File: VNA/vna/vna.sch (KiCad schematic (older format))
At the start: 4 parts, among them J1 USB_B_Micro, J2 Battery Cell Connection, J3 Pt1, J4 Pt2

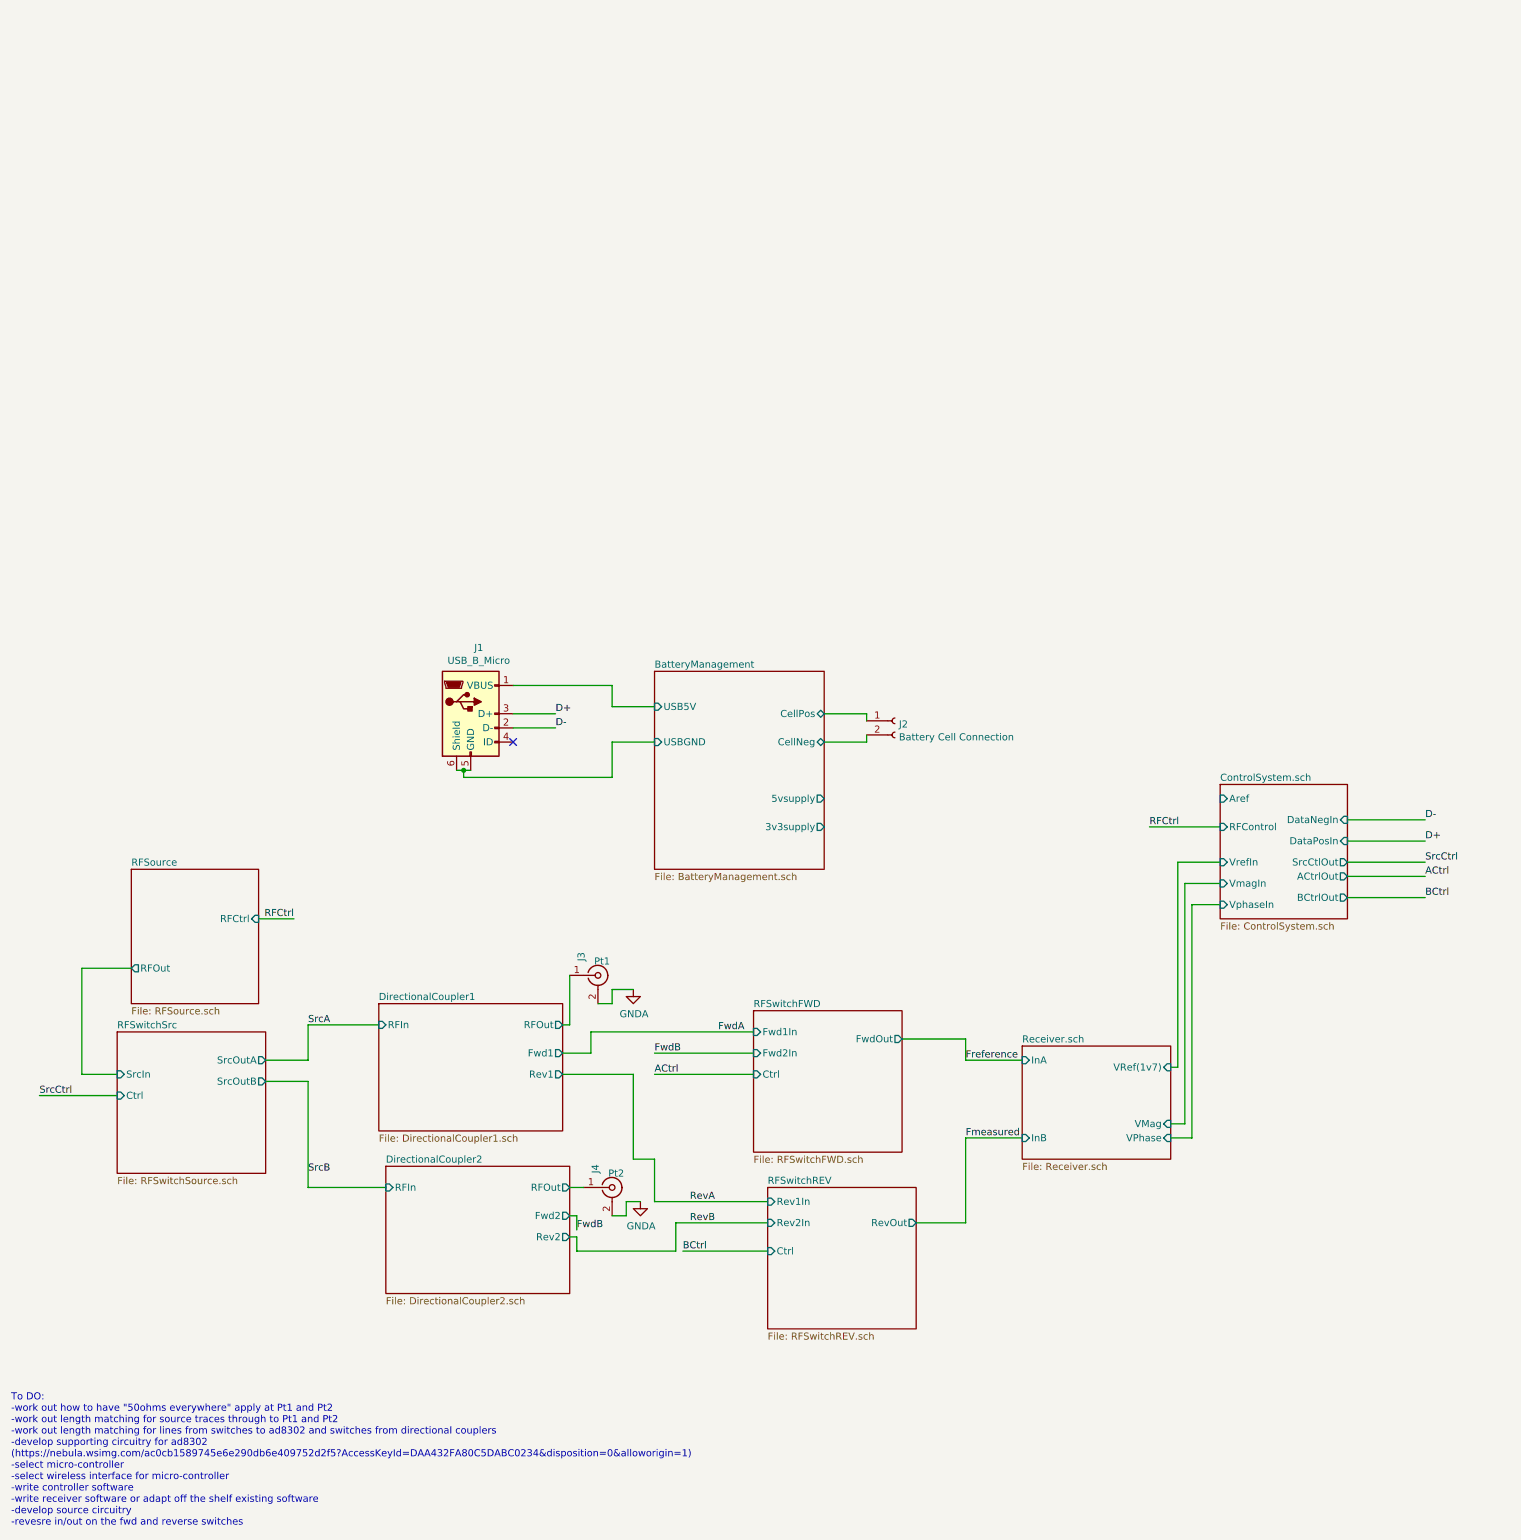
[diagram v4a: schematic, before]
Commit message: finished controller, chose compatible switches
controller and rf switches have been completed.

ToDo: finish filter design for RF Source, add auto gain control
ToDo: finish directional coupler footprints
ToDo: PCB Layout
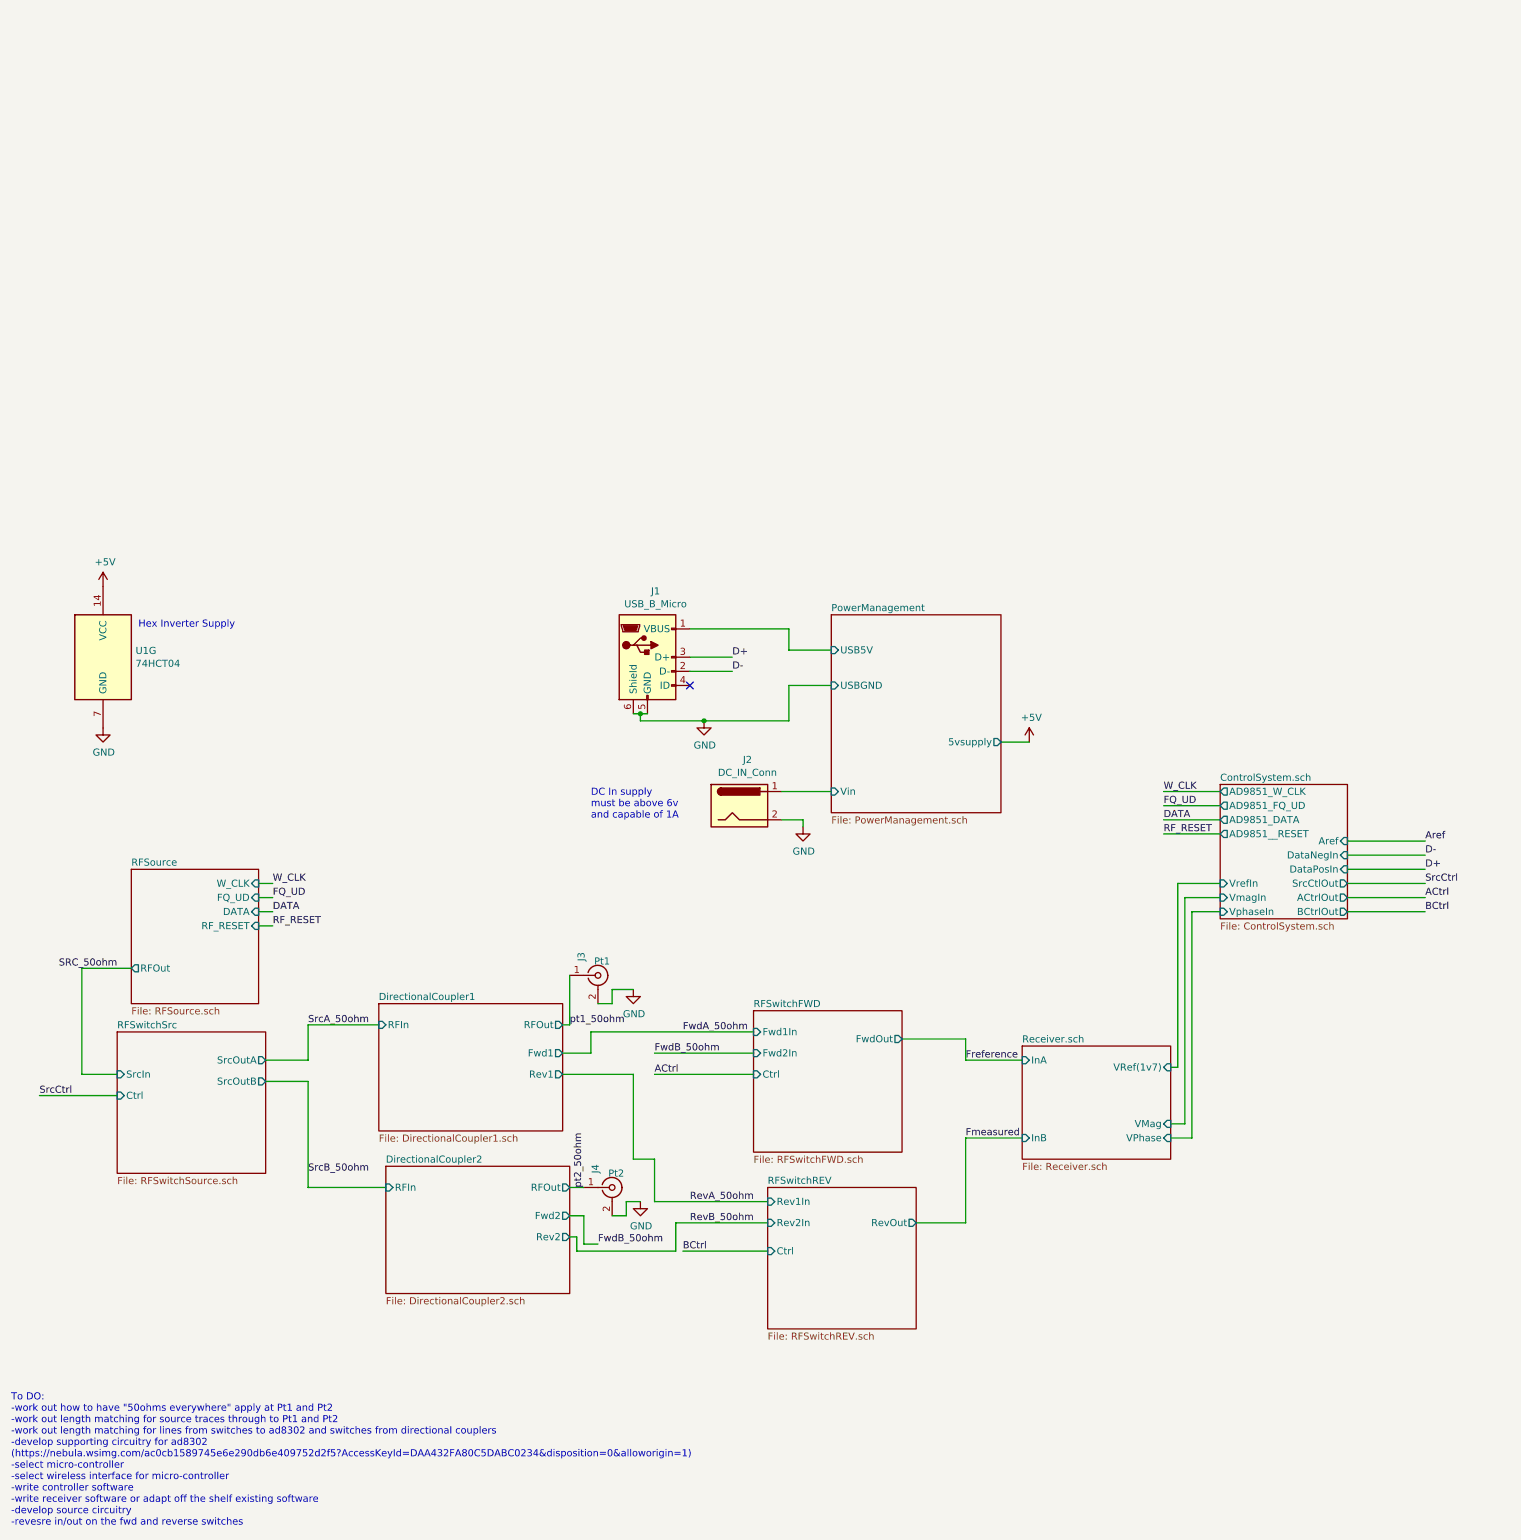
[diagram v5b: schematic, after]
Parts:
- removed J2: Battery Cell Connection, symbol Connector:Conn_01x02_Female
- added J2: DC_IN_Conn, Connector_BarrelJack:BarrelJack_Wuerth_6941xx301002, symbol Connector:Barrel_Jack
- added U1: 74HCT04, Package_SO:SOIC-14_3.9x8.7mm_P1.27mm, symbol 74xx:74HCT04
- J1: footprint (none) -> Connector_USB:USB_Micro-B_Amphenol_10103594-0001LF_Horizontal
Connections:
- net GNDA is gone; now on net GND: J3.2 (Ext), J4.2 (Ext)
- net BatteryManagement/USB5V renamed PowerManagement/USB5V
- net BatteryManagement/USBGND renamed GND
- net GND: now also J2.2, U1.7 (GND)
- net DirectionalCoupler1/RFOut renamed pt1_50ohm
- net DirectionalCoupler2/RFOut renamed pt2_50ohm
- new net +5V: U1.14 (VCC)
- new net PowerManagement/Vin: J2.1
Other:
- note added: "DC In supply \nmust be above 6v\nand capable of 1A"
- note added: "Hex Inverter Supply"
- moved on the sheet: J1

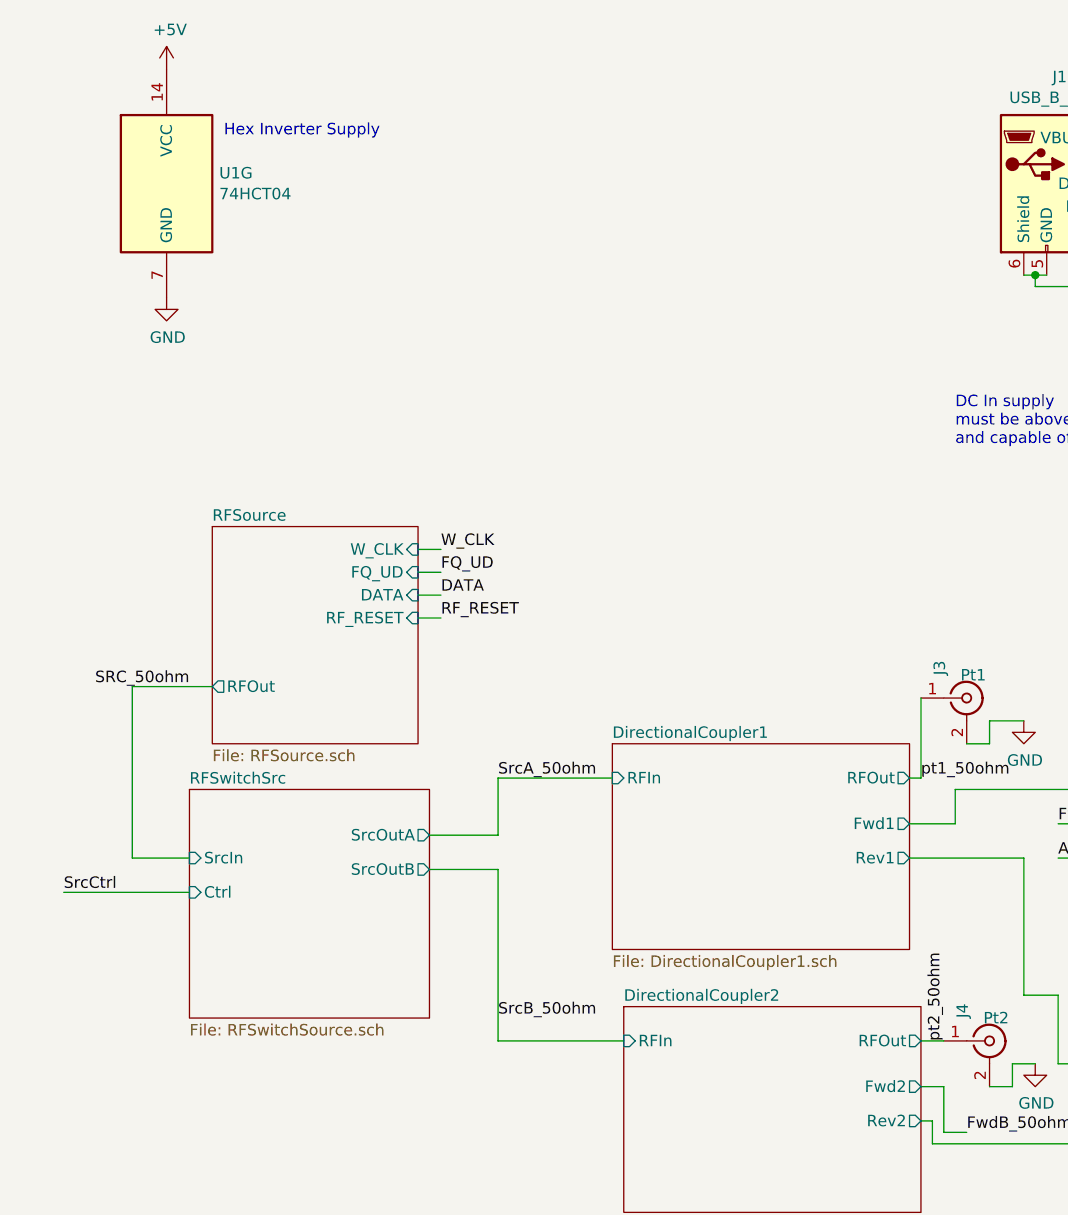
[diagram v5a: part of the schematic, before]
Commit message: custom footprint for couplers, added decoupling caps
added custom footprint for directional couplers - will need to verify it

added decoupling caps to ad9851
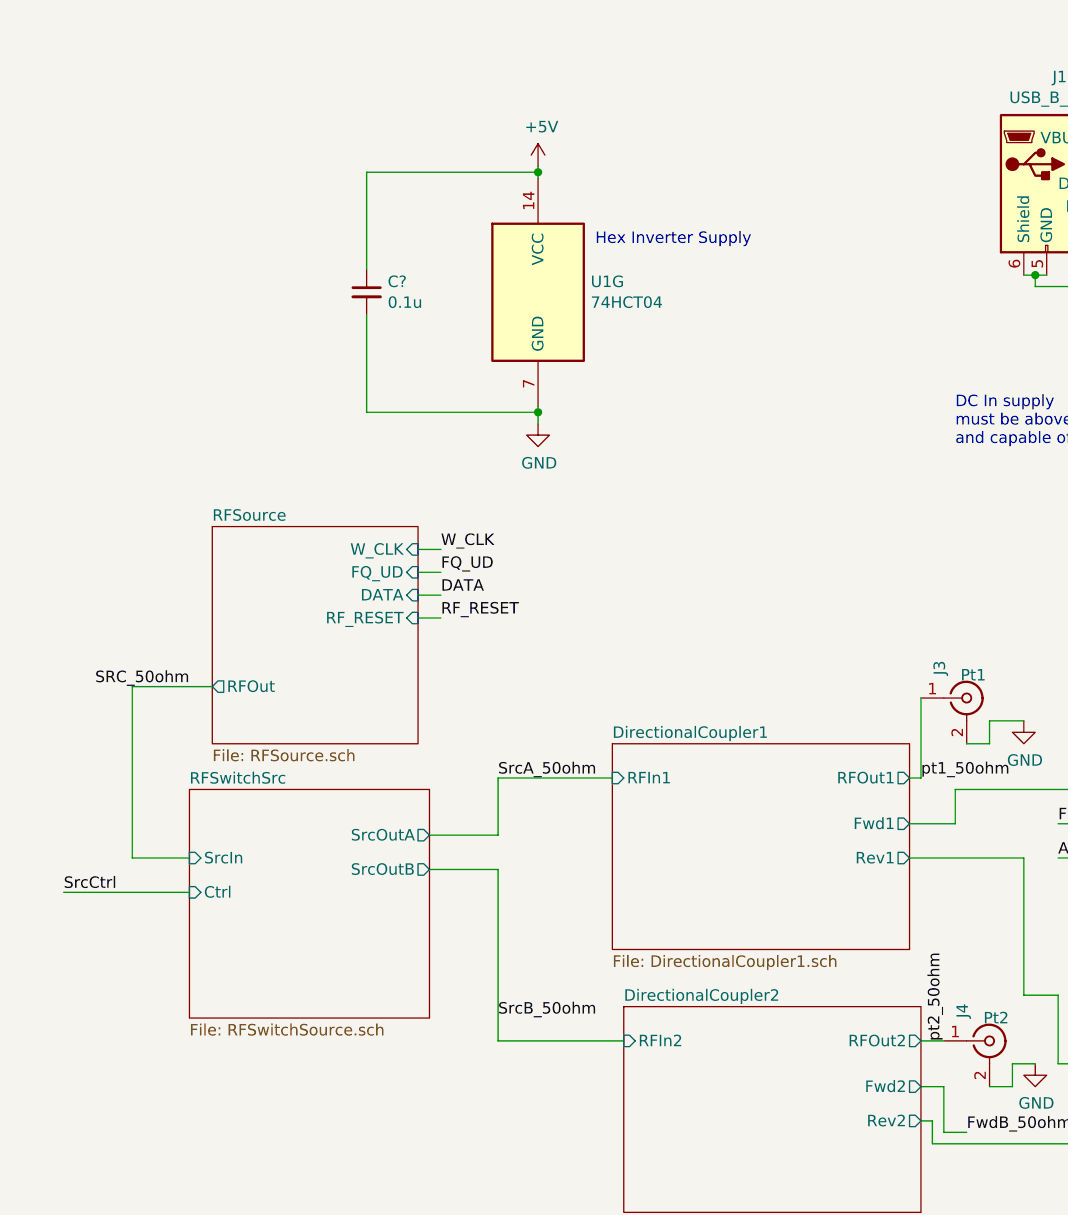
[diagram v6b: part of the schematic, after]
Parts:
- added C?: 0.1u, symbol Device:C_Small
- J3, J4: footprint (none) -> Connector_Coaxial:BNC_Amphenol_B6252HB-NPP3G-50_Horizontal
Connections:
- net +5V: now also C?.1
- net GND: now also C?.2
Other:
- moved on the sheet: U1G
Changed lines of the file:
@@
 F 0 "J3" V 4732 3750 50  0000 L CNN
 F 1 "Pt1" H 4823 3750 50  0000 L CNN
-F 2 "" H 4850 3650 50  0001 C CNN
+F 2 "Connector_Coaxial:BNC_Amphenol_B6252HB-NPP3G-50_Horizontal" H 4850 3650 50  0001 C CNN
 F 3 " ~" H 4850 3650 50  0001 C CNN
 	1    4850 3650
@@
 F0 "DirectionalCoupler1" 50
 F1 "DirectionalCoupler1.sch" 50
-F2 "RFIn" I L 3300 4000 50
-F3 "RFOut" O R 4600 4000 50
+F2 "RFOut1" O R 4600 4000 50
+F3 "RFIn1" I L 3300 4000 50
 F4 "Fwd1" O R 4600 4200 50
 F5 "Rev1" O R 4600 4350 50
-$EndSheet
-$Sheet
-S 3350 5000 1300 900
-U 5CC6A089
-F0 "DirectionalCoupler2" 50
-F1 "DirectionalCoupler2.sch" 50
-F2 "RFIn" I L 3350 5150 50
-F3 "RFOut" O R 4650 5150 50
-F4 "Fwd2" O R 4650 5350 50
-F5 "Rev2" O R 4650 5500 50
 $EndSheet
 $Sheet
@@
 F 0 "J4" V 4832 5250 50  0000 L CNN
 F 1 "Pt2" H 4923 5250 50  0000 L CNN
-F 2 "" H 4950 5150 50  0001 C CNN
+F 2 "Connector_Coaxial:BNC_Amphenol_B6252HB-NPP3G-50_Horizontal" H 4950 5150 50  0001 C CNN
 F 3 " ~" H 4950 5150 50  0001 C CNN
 	1    4950 5150
@@
 L 74xx:74HCT04 U1
 U 7 1 5D8669BB
-P 1350 1400
-F 0 "U1" H 1580 1446 50  0000 L CNN
-F 1 "74HCT04" H 1580 1355 50  0000 L CNN
-F 2 "Package_SO:SOIC-14_3.9x8.7mm_P1.27mm" H 1350 1400 50  0001 C CNN
-F 3 "https://assets.nexperia.com/documents/data-sheet/74HC_HCT04.pdf" H 1350 1400 50  0001 C CNN
-	7    1350 1400
+P 2975 1875
+F 0 "U1" H 3205 1921 50  0000 L CNN
+F 1 "74HCT04" H 3205 1830 50  0000 L CNN
+F 2 "Package_SO:SOIC-14_3.9x8.7mm_P1.27mm" H 2975 1875 50  0001 C CNN
+F 3 "https://assets.nexperia.com/documents/data-sheet/74HC_HCT04.pdf" H 2975 1875 50  0001 C CNN
+	7    2975 1875
 	1    0    0    -1
 $EndComp
@@
 L power:GND #PWR03
 U 1 1 5D86818F
-P 1350 1900
-F 0 "#PWR03" H 1350 1650 50  0001 C CNN
-F 1 "GND" H 1355 1727 50  0000 C CNN
-F 2 "" H 1350 1900 50  0001 C CNN
-F 3 "" H 1350 1900 50  0001 C CNN
-	1    1350 1900
+P 2975 2450
+F 0 "#PWR03" H 2975 2200 50  0001 C CNN
+F 1 "GND" H 2980 2277 50  0000 C CNN
+F 2 "" H 2975 2450 50  0001 C CNN
+F 3 "" H 2975 2450 50  0001 C CNN
+	1    2975 2450
 	1    0    0    -1
 $EndComp
@@
 L power:+5V #PWR?
 U 1 1 5D869326
-P 1350 900
+P 2975 1325
 AR Path="/5CD1CF30/5D869326" Ref="#PWR?"  Part="1"
 AR Path="/5D869326" Ref="#PWR01"  Part="1"
-F 0 "#PWR01" H 1350 750 50  0001 C CNN
-F 1 "+5V" H 1365 1073 50  0000 C CNN
-F 2 "" H 1350 900 50  0001 C CNN
-F 3 "" H 1350 900 50  0001 C CNN
-	1    1350 900
+F 0 "#PWR01" H 2975 1175 50  0001 C CNN
+F 1 "+5V" H 2990 1498 50  0000 C CNN
+F 2 "" H 2975 1325 50  0001 C CNN
+F 3 "" H 2975 1325 50  0001 C CNN
+	1    2975 1325
 	1    0    0    -1
 $EndComp
@@
 Text Notes 4800 2550 0    50   ~ 0
 DC In supply \nmust be above 6v\nand capable of 1A
-Text Notes 1600 1200 0    50   ~ 0
+Text Notes 3225 1675 0    50   ~ 0
 Hex Inverter Supply
 Wire Wire Line
@@
 Wire Wire Line
 	2450 3300 2550 3300
+$Sheet
+S 3350 5000 1300 900
+U 5CC6A089
+F0 "DirectionalCoupler2" 50
+F1 "DirectionalCoupler2.sch" 50
+F2 "Fwd2" O R 4650 5350 50
+F3 "Rev2" O R 4650 5500 50
+F4 "RFOut2" O R 4650 5150 50
+F5 "RFIn2" I L 3350 5150 50
+$EndSheet
+$Comp
+L Device:C_Small C?
+U 1 1 5D96EE93
+P 2225 1875
+F 0 "C?" H 2317 1921 50  0000 L CNN
+F 1 "0.1u" H 2317 1830 50  0000 L CNN
+F 2 "" H 2225 1875 50  0001 C CNN
+F 3 "~" H 2225 1875 50  0001 C CNN
+	1    2225 1875
+	1    0    0    -1
+$EndComp
+Wire Wire Line
+	2975 2450 2975 2400
+Wire Wire Line
+	2975 1325 2975 1350
+Wire Wire Line
+	2225 1775 2225 1350
+Wire Wire Line
+	2225 1350 2975 1350
+Connection ~ 2975 1350
+Wire Wire Line
+	2975 1350 2975 1375
+Wire Wire Line
+	2225 1975 2225 2400
+Wire Wire Line
+	2225 2400 2975 2400
+Connection ~ 2975 2400
+Wire Wire Line
+	2975 2400 2975 2375
 $EndSCHEMATC

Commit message: beginning pcb layout
pcb layout process begun
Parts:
- C30: renamed from C?; footprint (none) -> Capacitor_SMD:C_1206_3216Metric_Pad1.42x1.75mm_HandSolder
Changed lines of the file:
@@
 $EndSheet
 $Comp
-L Device:C_Small C?
+L Device:C_Small C30
 U 1 1 5D96EE93
 P 2225 1875
-F 0 "C?" H 2317 1921 50  0000 L CNN
+F 0 "C30" H 2317 1921 50  0000 L CNN
 F 1 "0.1u" H 2317 1830 50  0000 L CNN
-F 2 "" H 2225 1875 50  0001 C CNN
+F 2 "Capacitor_SMD:C_1206_3216Metric_Pad1.42x1.75mm_HandSolder" H 2225 1875 50  0001 C CNN
 F 3 "~" H 2225 1875 50  0001 C CNN
 	1    2225 1875
